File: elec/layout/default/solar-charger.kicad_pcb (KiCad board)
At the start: 2 copper layers, 225.7 x 100.8 mm, 0 parts

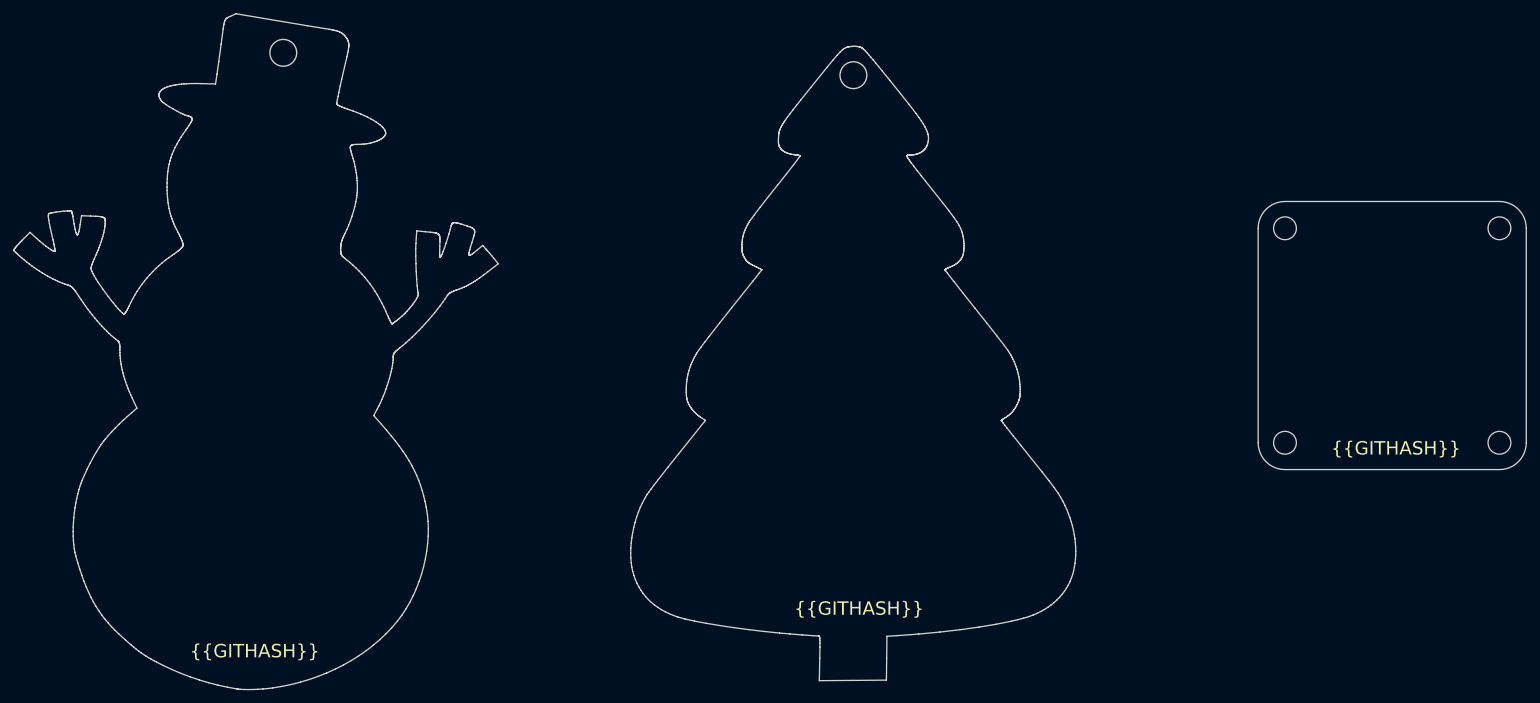
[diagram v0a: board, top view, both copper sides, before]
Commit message: solar side done
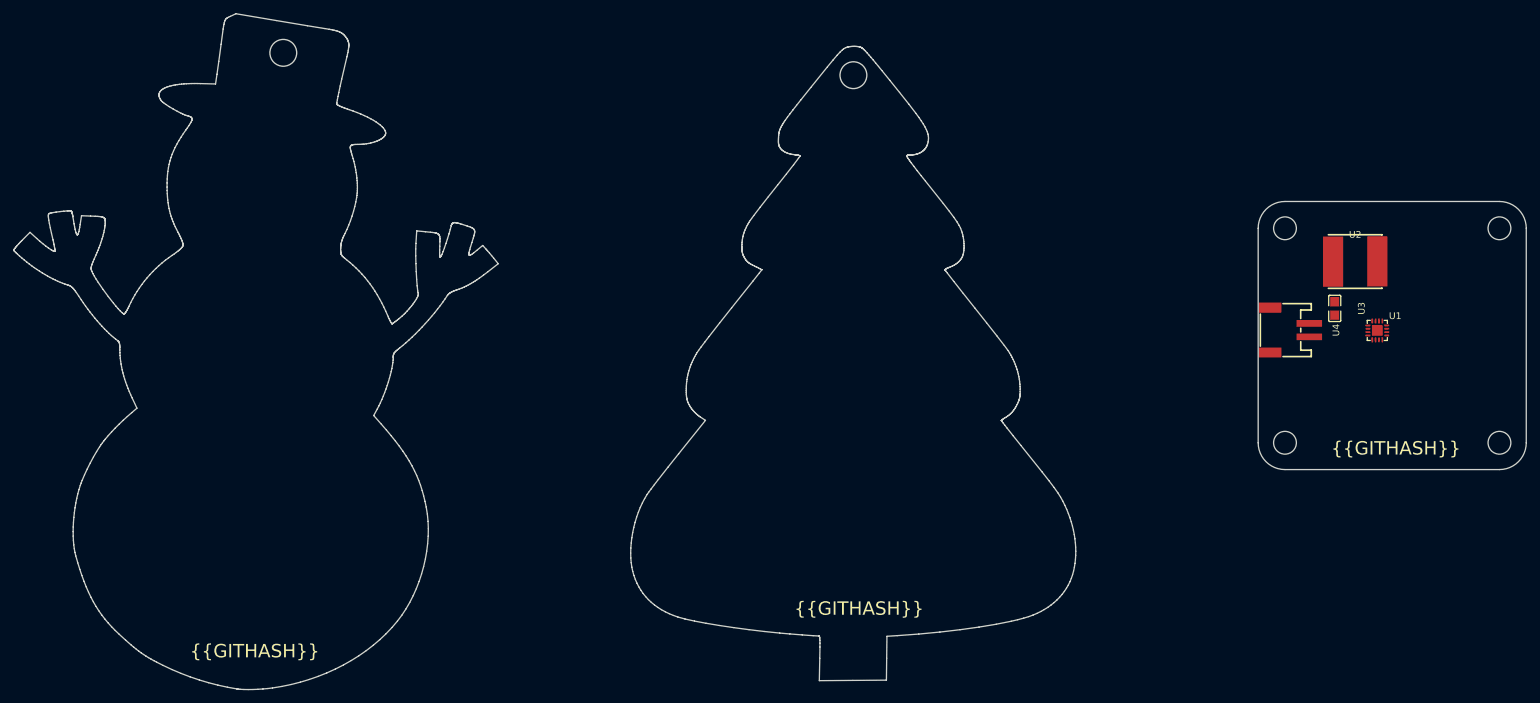
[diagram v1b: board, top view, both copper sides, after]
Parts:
- added U1: , lib:VQFN-16_L3.0-W3.0-P0.50-TL-EP, F.Cu at (239.4, 97.0)
- added U2: , lib:IND-SMD_L8.0-W8.0_FNR80XXS, F.Cu at (236.1, 86.8)
- added U3: , lib:C0805, F.Cu at (233.0, 93.7)
- added U4: , lib:CONN-SMD_P2.00_S2B-PH-SM4-TB-LF-SN, F.Cu at (226.3, 97.0)
